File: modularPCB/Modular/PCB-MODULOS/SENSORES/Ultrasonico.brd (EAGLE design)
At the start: 22 x 24 mm, 5 parts

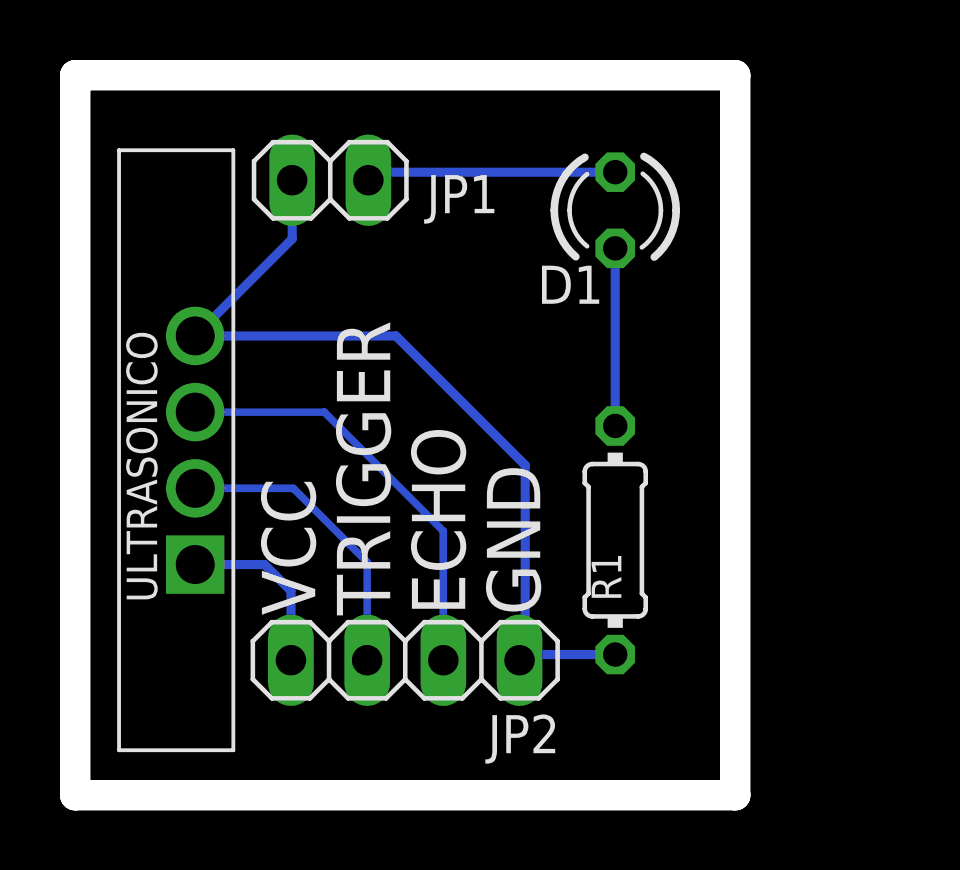
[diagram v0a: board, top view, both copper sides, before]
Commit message: Se agregaron brd de la ultima actualización
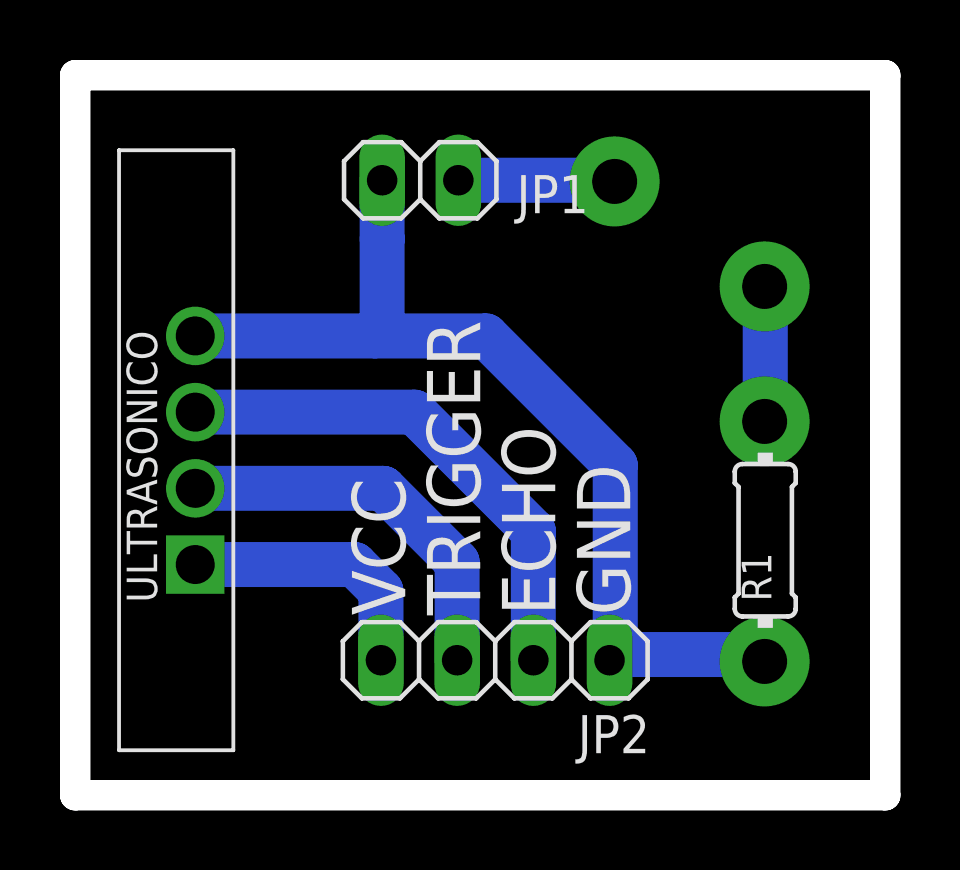
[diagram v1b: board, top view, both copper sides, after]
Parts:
- removed D1: (no value), led:LED3MM
- moved R1 5.00 mm to (23.0, 8.50)
- moved JP1 3.00 mm to (11.5, 20.5)
- moved JP2 3.00 mm to (14.0, 4.50)
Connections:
- removed net N$1: D1.K, R1.2
- net PULSO-ULTRASONICO: now also R1.2; no longer D1.A
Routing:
- net N$1: track 5.92 -> 0.00 mm, vias 0 -> 1
- net GND: track 29.3 -> 33.0 mm
- net TRIGGER: track 10.0 -> 13.0 mm
- net VCC: track 5.86 -> 8.86 mm
- net ECHO: track 14.2 -> 17.2 mm
- net PULSO-ULTRASONICO: track 8.34 -> 9.92 mm
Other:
- board size 22 x 24 mm -> 27 x 24 mm
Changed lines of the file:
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@@
 <board>
 <plain>
-<wire x1="0" y1="0" x2="22" y2="0" width="1.016" layer="20"/>
-<wire x1="22" y1="0" x2="22" y2="24" width="1.016" layer="20"/>
-<wire x1="22" y1="24" x2="0" y2="24" width="1.016" layer="20"/>
+<wire x1="0" y1="0" x2="27" y2="0" width="1.016" layer="20"/>
+<wire x1="27" y1="0" x2="27" y2="24" width="1.016" layer="20"/>
+<wire x1="27" y1="24" x2="0" y2="24" width="1.016" layer="20"/>
 <wire x1="0" y1="24" x2="0" y2="0" width="1.016" layer="20"/>
-<text x="8" y="6" size="1.778" layer="21" rot="R90">VCC</text>
-<text x="10.5" y="6" size="1.778" layer="21" rot="R90">TRIGGER</text>
-<text x="13" y="6" size="1.778" layer="21" rot="R90">ECHO</text>
-<text x="15.5" y="6" size="1.778" layer="21" rot="R90">GND</text>
-<dimension x1="22" y1="24" x2="0" y2="24" x3="11" y3="26.5" textsize="1.778" layer="48"/>
-<dimension x1="22" y1="0" x2="22" y2="24" x3="25.5" y3="12" textsize="1.778" layer="48"/>
+<text x="11" y="6" size="1.778" layer="21" rot="R90">VCC</text>
+<text x="13.5" y="6" size="1.778" layer="21" rot="R90">TRIGGER</text>
+<text x="16" y="6" size="1.778" layer="21" rot="R90">ECHO</text>
+<text x="18.5" y="6" size="1.778" layer="21" rot="R90">GND</text>
+<dimension x1="27" y1="24" x2="0" y2="24" x3="13.5" y3="26.5" textsize="1.778" layer="48"/>
+<dimension x1="27" y1="0" x2="27" y2="24" x3="28.5" y3="12" textsize="1.778" layer="48"/>
 </plain>
 <attributes>
@@
 </autorouter>
 <elements>
-<element name="JP1" library="pinhead" library_urn="urn:adsk.eagle:library:325" package="1X02" package3d_urn="urn:adsk.eagle:package:22435/2" value="" x="8.5" y="20.5" smashed="yes" rot="R180">
-<attribute name="NAME" x="14.1162" y="20.6712" size="1.27" layer="25" ratio="10" rot="R180"/>
-<attribute name="POPULARITY" value="98" x="-8.01" y="38.28" size="1.778" layer="27" rot="R180" display="off"/>
-<attribute name="VALUE" x="11.04" y="23.675" size="1.27" layer="27" rot="R180"/>
+<element name="JP1" library="pinhead" library_urn="urn:adsk.eagle:library:325" package="1X02" package3d_urn="urn:adsk.eagle:package:22435/2" value="" x="11.5" y="20.5" smashed="yes" rot="R180">
+<attribute name="NAME" x="17.1162" y="20.6712" size="1.27" layer="25" ratio="10" rot="R180"/>
+<attribute name="POPULARITY" value="98" x="-5.01" y="38.28" size="1.778" layer="27" rot="R180" display="off"/>
+<attribute name="VALUE" x="14.04" y="23.675" size="1.27" layer="27" rot="R180"/>
 </element>
-<element name="JP2" library="pinhead" library_urn="urn:adsk.eagle:library:325" package="1X04" package3d_urn="urn:adsk.eagle:package:22407/2" value="" x="11" y="4.5" smashed="yes" rot="R180">
-<attribute name="NAME" x="16.1562" y="2.6712" size="1.27" layer="25" ratio="10" rot="R180"/>
-<attribute name="POPULARITY" value="91" x="-8.05" y="15.93" size="1.778" layer="27" rot="R180" display="off"/>
-<attribute name="VALUE" x="16.08" y="7.675" size="1.27" layer="27" rot="R180"/>
+<element name="JP2" library="pinhead" library_urn="urn:adsk.eagle:library:325" package="1X04" package3d_urn="urn:adsk.eagle:package:22407/2" value="" x="14" y="4.5" smashed="yes" rot="R180">
+<attribute name="NAME" x="19.1562" y="2.6712" size="1.27" layer="25" ratio="10" rot="R180"/>
+<attribute name="POPULARITY" value="91" x="-5.05" y="15.93" size="1.778" layer="27" rot="R180" display="off"/>
+<attribute name="VALUE" x="19.08" y="7.675" size="1.27" layer="27" rot="R180"/>
 </element>
-<element name="D1" library="led" library_urn="urn:adsk.eagle:library:259" package="LED3MM" package3d_urn="urn:adsk.eagle:package:15797/1" value="" x="18" y="19.5" smashed="yes" rot="R270">
-<attribute name="NAME" x="15.405" y="16.381" size="1.27" layer="25" ratio="10"/>
-<attribute name="POPULARITY" value="97" x="0.22" y="-7.17" size="1.778" layer="27" rot="R270" display="off"/>
-<attribute name="VALUE" x="16.349" y="17.595" size="1.27" layer="27" ratio="10" rot="R270"/>
-</element>
-<element name="R1" library="rcl" library_urn="urn:adsk.eagle:library:334" package="0204/7" package3d_urn="urn:adsk.eagle:package:23498/2" value="220" x="18" y="8.5" smashed="yes" rot="R90">
-<attribute name="NAME" x="18.2046" y="6.46" size="0.9906" layer="25" ratio="10" rot="R90"/>
-<attribute name="POPULARITY" value="79" x="40.86" y="26.28" size="1.778" layer="27" rot="R90" display="off"/>
-<attribute name="SPICEPREFIX" value="R" x="40.86" y="26.28" size="1.778" layer="27" rot="R90" display="off"/>
-<attribute name="VALUE" x="18.4826" y="8.3744" size="0.9906" layer="27" ratio="10" rot="R90"/>
+<element name="R1" library="rcl" library_urn="urn:adsk.eagle:library:334" package="0204/7" package3d_urn="urn:adsk.eagle:package:23498/2" value="220" x="23" y="8.5" smashed="yes" rot="R90">
+<attribute name="NAME" x="23.2046" y="6.46" size="0.9906" layer="25" ratio="10" rot="R90"/>
+<attribute name="POPULARITY" value="79" x="45.86" y="26.28" size="1.778" layer="27" rot="R90" display="off"/>
+<attribute name="SPICEPREFIX" value="R" x="45.86" y="26.28" size="1.778" layer="27" rot="R90" display="off"/>
+<attribute name="VALUE" x="23.4826" y="8.3744" size="0.9906" layer="27" ratio="10" rot="R90"/>
 </element>
 <element name="U$1" library="MODULAR" package="ULTRASONICO" value="ULTRASONICO" x="4" y="11.5" smashed="yes" rot="R90"/>
@@
 <contactref element="U$1" pad="GND"/>
 <contactref element="JP2" pad="1"/>
-<wire x1="14.81" y1="4.5" x2="15" y2="4.5" width="0.3048" layer="16"/>
-<wire x1="4" y1="15.31" x2="10.69" y2="15.31" width="0.3048" layer="16"/>
-<wire x1="15" y1="11" x2="15" y2="4.5" width="0.3048" layer="16"/>
-<wire x1="10.69" y1="15.31" x2="15" y2="11" width="0.3048" layer="16"/>
-<wire x1="14.81" y1="4.5" x2="15" y2="4.69" width="0.3048" layer="16"/>
-<wire x1="15" y1="4.69" x2="18" y2="4.69" width="0.3048" layer="16"/>
-<wire x1="7.23" y1="20.5" x2="7.23" y2="18.54" width="0.3048" layer="16"/>
-<wire x1="7.23" y1="18.54" x2="4" y2="15.31" width="0.3048" layer="16"/>
+<wire x1="17.81" y1="4.5" x2="18" y2="4.5" width="1.5" layer="16"/>
+<wire x1="4" y1="15.31" x2="10" y2="15.31" width="1.5" layer="16"/>
+<wire x1="10" y1="15.31" x2="13.69" y2="15.31" width="1.5" layer="16"/>
+<wire x1="18" y1="11" x2="18" y2="4.5" width="1.5" layer="16"/>
+<wire x1="13.69" y1="15.31" x2="18" y2="11" width="1.5" layer="16"/>
+<wire x1="17.81" y1="4.5" x2="18" y2="4.69" width="1.5" layer="16"/>
+<wire x1="18" y1="4.69" x2="23" y2="4.69" width="1.5" layer="16"/>
+<wire x1="10.23" y1="20.5" x2="10.23" y2="18.54" width="1.5" layer="16"/>
+<wire x1="10.23" y1="18.54" x2="10.23" y2="15.54" width="1.5" layer="16"/>
+<wire x1="10.23" y1="15.54" x2="10" y2="15.31" width="0.1524" layer="16"/>
 </signal>
 <signal name="PULSO-ULTRASONICO">
-<contactref element="D1" pad="A"/>
 <contactref element="JP1" pad="1"/>
-<wire x1="9.77" y1="20.5" x2="10.04" y2="20.77" width="0.3048" layer="16"/>
-<wire x1="10.04" y1="20.77" x2="18" y2="20.77" width="0.3048" layer="16"/>
-</signal>
-<signal name="N$1">
-<contactref element="D1" pad="K"/>
 <contactref element="R1" pad="2"/>
-<wire x1="18" y1="18.23" x2="18" y2="12.31" width="0.3048" layer="16"/>
+<wire x1="12.77" y1="20.5" x2="18" y2="20.5" width="1.5" layer="16"/>
+<wire x1="23" y1="12.31" x2="23" y2="17" width="1.5" layer="16"/>
+<wire x1="23" y1="17" x2="18" y2="20.5" width="0" layer="19" extent="16-16"/>
 </signal>
 <signal name="VCC">
 <contactref element="JP2" pad="4"/>
 <contactref element="U$1" pad="VCC"/>
-<wire x1="4" y1="7.69" x2="6.31" y2="7.69" width="0.3048" layer="16"/>
-<wire x1="7.19" y1="6.81" x2="7.19" y2="4.5" width="0.3048" layer="16"/>
-<wire x1="6.31" y1="7.69" x2="7.19" y2="6.81" width="0.3048" layer="16"/>
+<wire x1="4" y1="7.69" x2="9.31" y2="7.69" width="1.5" layer="16"/>
+<wire x1="10.19" y1="6.81" x2="10.19" y2="4.5" width="1.5" layer="16"/>
+<wire x1="9.31" y1="7.69" x2="10.19" y2="6.81" width="1.5" layer="16"/>
 </signal>
 <signal name="TRIGGER">
 <contactref element="U$1" pad="TRIG"/>
 <contactref element="JP2" pad="3"/>
-<wire x1="9.73" y1="4.5" x2="9.73" y2="7.77" width="0.254" layer="16"/>
-<wire x1="7.27" y1="10.23" x2="4" y2="10.23" width="0.254" layer="16"/>
-<wire x1="9.73" y1="7.77" x2="7.27" y2="10.23" width="0.254" layer="16"/>
+<wire x1="12.73" y1="4.5" x2="12.73" y2="7.77" width="1.5" layer="16"/>
+<wire x1="10.27" y1="10.23" x2="4" y2="10.23" width="1.5" layer="16"/>
+<wire x1="12.73" y1="7.77" x2="10.27" y2="10.23" width="1.5" layer="16"/>
 </signal>
 <signal name="ECHO">
 <contactref element="JP2" pad="2"/>
 <contactref element="U$1" pad="ECHO"/>
-<wire x1="12.27" y1="4.5" x2="12.27" y2="8.8047375" width="0.254" layer="16"/>
-<wire x1="12.27" y1="8.8047375" x2="8.3047375" y2="12.77" width="0.254" layer="16"/>
-<wire x1="8.3047375" y1="12.77" x2="4" y2="12.77" width="0.254" layer="16"/>
+<wire x1="15.27" y1="4.5" x2="15.27" y2="8.8047375" width="1.5" layer="16"/>
+<wire x1="15.27" y1="8.8047375" x2="11.3047375" y2="12.77" width="1.5" layer="16"/>
+<wire x1="11.3047375" y1="12.77" x2="4" y2="12.77" width="1.5" layer="16"/>
+</signal>
+<signal name="N$1">
+<via x="17.98" y="20.46" extent="1-16" drill="1.5" diameter="3"/>
+</signal>
+<signal name="PULSO-GALGA">
+<via x="22.98" y="16.96" extent="1-16" drill="1.5" diameter="3"/>
+<via x="22.98" y="12.46" extent="1-16" drill="1.5" diameter="3"/>
+<via x="22.98" y="4.46" extent="1-16" drill="1.5" diameter="3"/>
+<wire x1="22.98" y1="12.46" x2="22.98" y2="16.96" width="0" layer="19" extent="1-1"/>
+<wire x1="22.98" y1="4.46" x2="22.98" y2="12.46" width="0" layer="19" extent="1-1"/>
 </signal>
 </signals>
